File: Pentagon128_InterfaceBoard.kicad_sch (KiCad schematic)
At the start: 35 parts, among them J1 DIN41612_02x32_AB, J10 Tape Out, J11 Tape In, J12 Mini-DIN-6, J13 Conn_02x05_Odd_Even ATmega Pr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, J14 Barrel_Jack_Switch, J2 Conn_02x03_Odd_Even ATmega Pr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, J3 Conn_02x08_Odd_Even Ext Keyb, J4 Conn_02x05_Odd_Even Kempston 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, J5 DE9_Plug Kempston Out SMD, J6 DE15_Plug_HighDensity VGA CRT, J7 Conn_01x04 FDD Power, J8 Conn_01x04 Audio In, J9 AudioJack3, Q1 Q_NPN_BCE, Q2 Q_NPN_BCE, Q3 Q_NPN_BCE, Q4 Q_NPN_BCE, U1 MT8816 PLCC44, U2 ATmega168PA-A

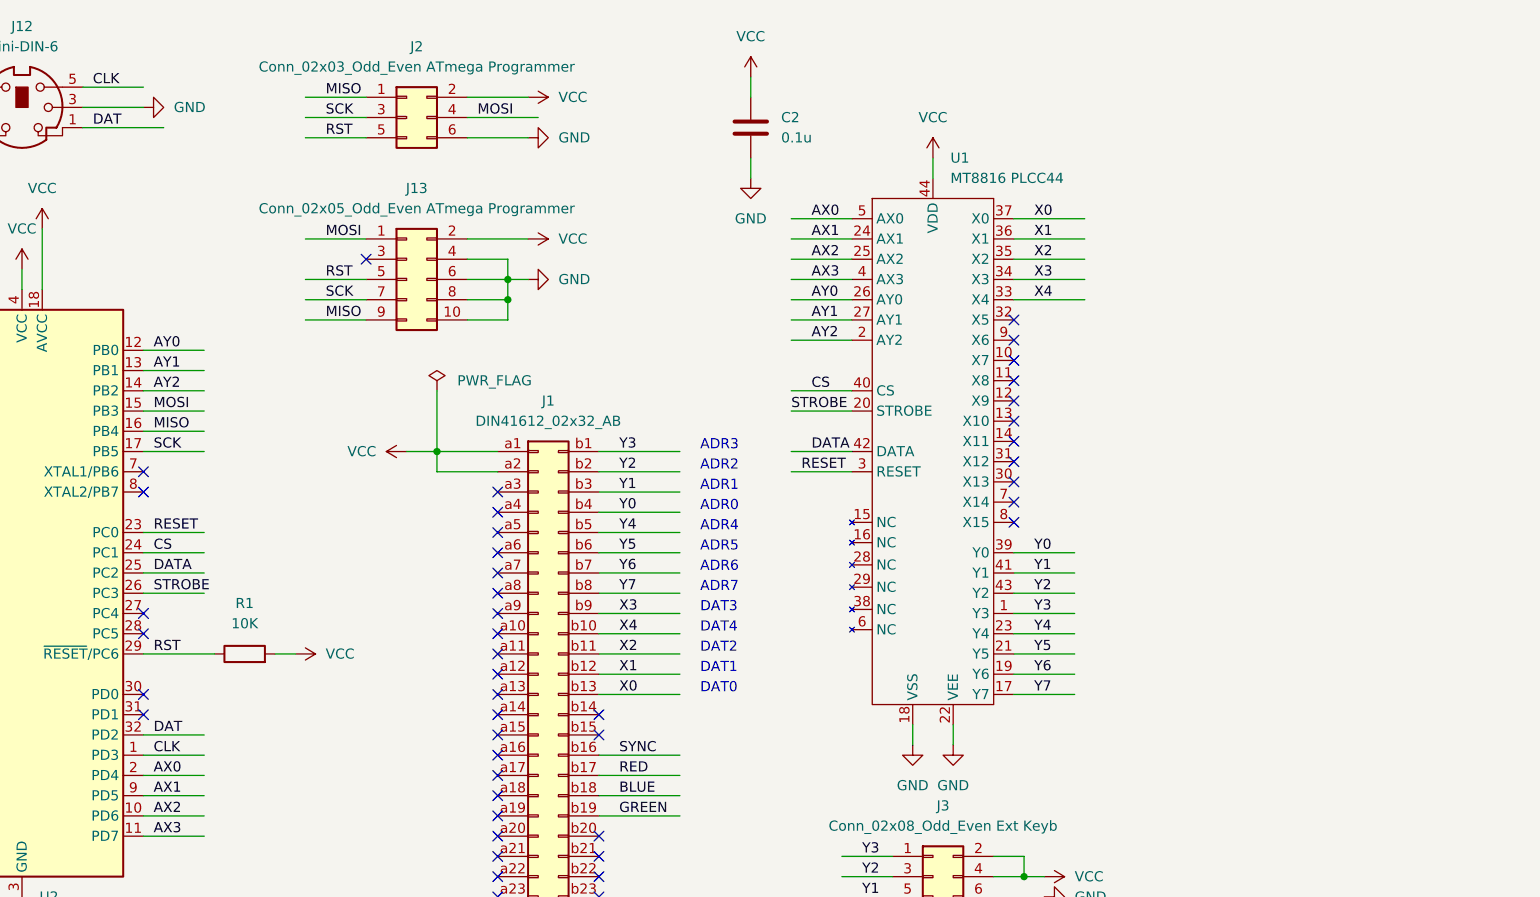
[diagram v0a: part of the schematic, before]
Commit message: Intermediate variant based on review feedback. Added SN74LS07 oped drain buffers for switch matrix data lines output (questionable). Changes based on "AVR Microcontroller Hardware Design Considerations": - Blocking capacitor for ATmega moved close to power input pins, removed side VCC / GND connections. Not implemented: separate blocking caps for AVCC and all power pins pairs. - Added optional capacitor on ATmega RESET line connected to GND. Removed useless blocking capacitor for MT8816. Removed (possibly) useless electrolytic capacitors from PCB near ATmega and FDC Power connector.
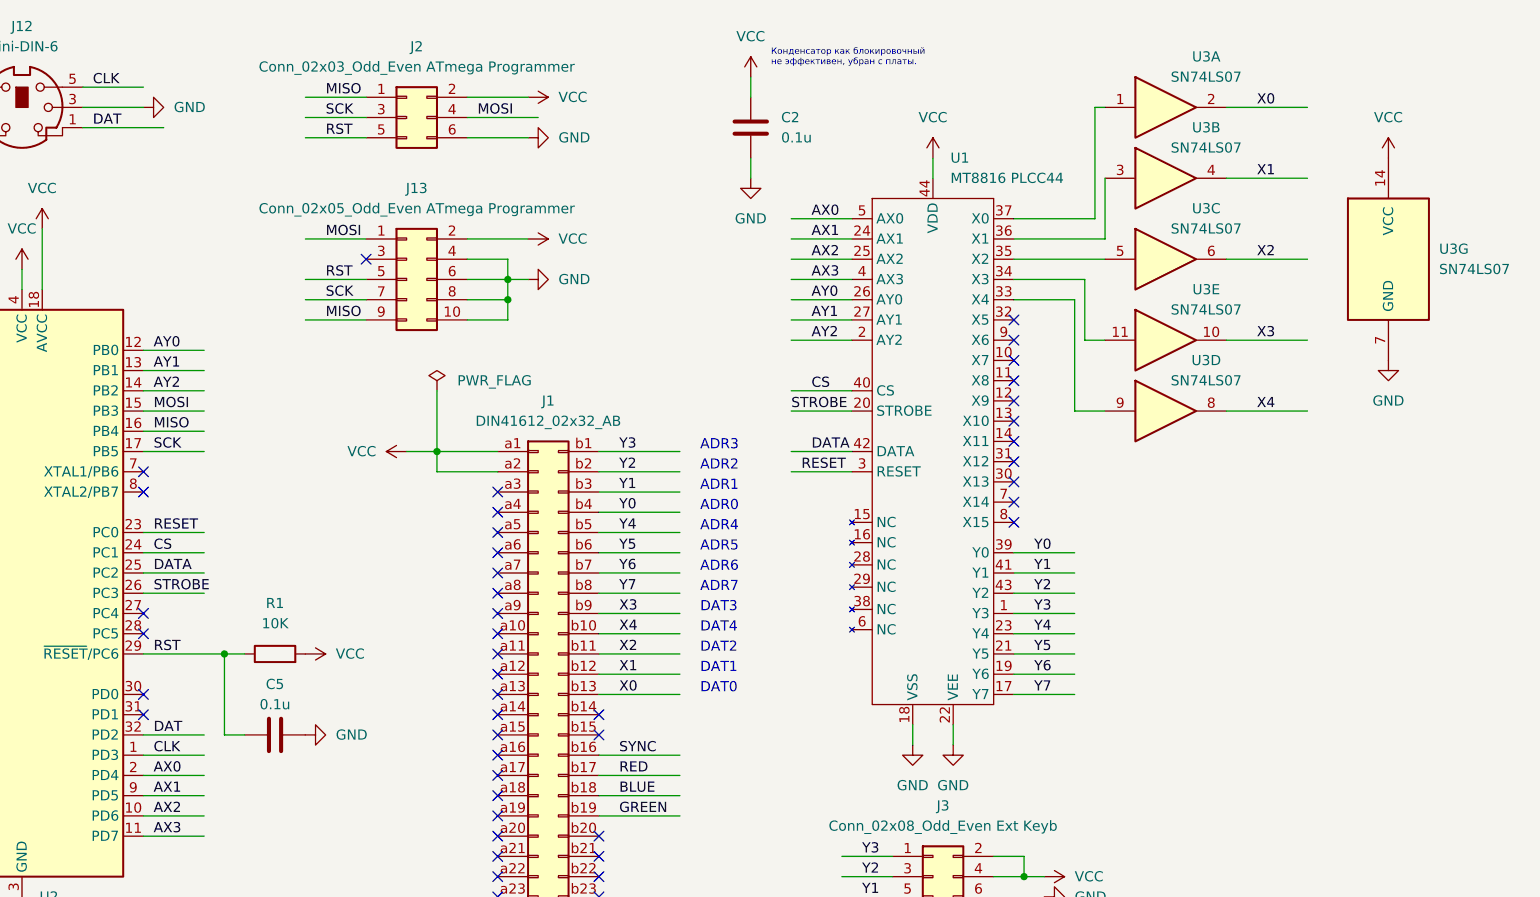
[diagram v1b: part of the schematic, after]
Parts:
- added C5: 0.1u, Capacitor_SMD:C_1206_3216Metric_Pad1.33x1.80mm_HandSolder, symbol Device:C
- added U3: SN74LS07, Package_SO:SOIC-14_3.9x8.7mm_P1.27mm, symbol 74xx:SN74LS07
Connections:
- net GND: now also C5.2, U3.7 (GND)
- net RST: now also C5.1
- net VCC: now also U3.14 (VCC)
- net X0: now also U3.2; no longer U1.37 (X0)
- net X1: now also U3.4; no longer U1.36 (X1)
- net X2: now also U3.6; no longer U1.35 (X2)
- net X3: now also U3.10; no longer U1.34 (X3)
- net X4: now also U3.8; no longer U1.33 (X4)
- new net: U1.37 (X0), U3.1
- new net: U1.35 (X2), U3.5
- new net: U1.33 (X4), U3.9
- new net: U1.34 (X3), U3.11
- new net: U1.36 (X1), U3.3
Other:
- note added: "Конденсатор как блокировочный не эффективен, убран с платы."
- moved on the sheet: R1

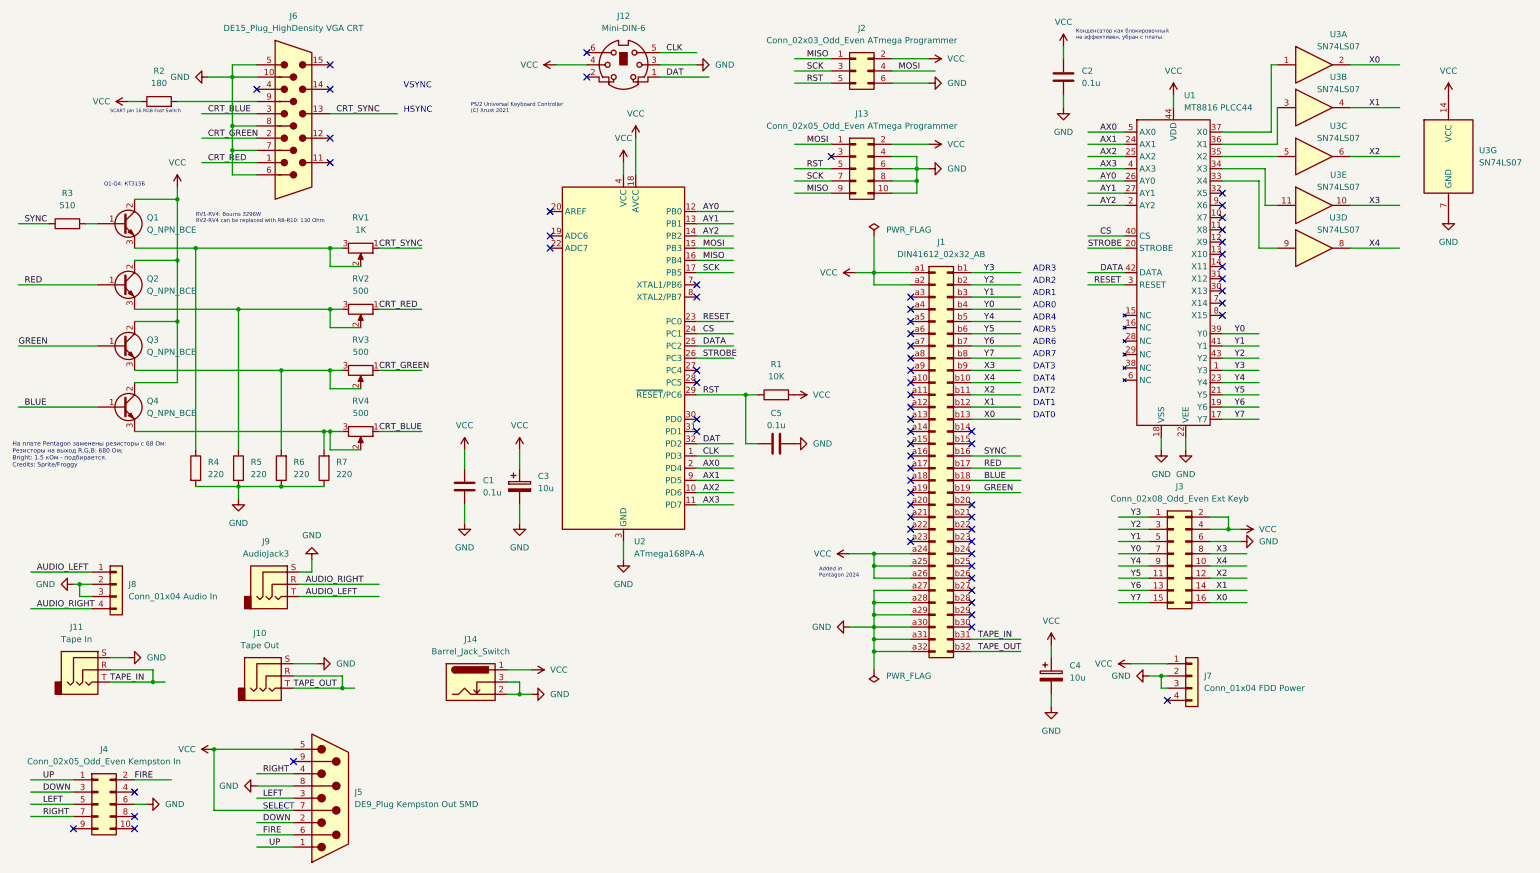
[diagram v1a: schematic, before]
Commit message: Remove SN74LS07 data bus buffer from schematic and PCB, considering MT8816 switches as switches connecting logical "0" from address bus line to keyboard data bus pulled to "1" (VCC) via pull-up resistors. There is no direct connections of address bus lines to VCC ("1") because of diodes.
Re-enumerate capacitors.
Remove electrolytic capacitors from board.
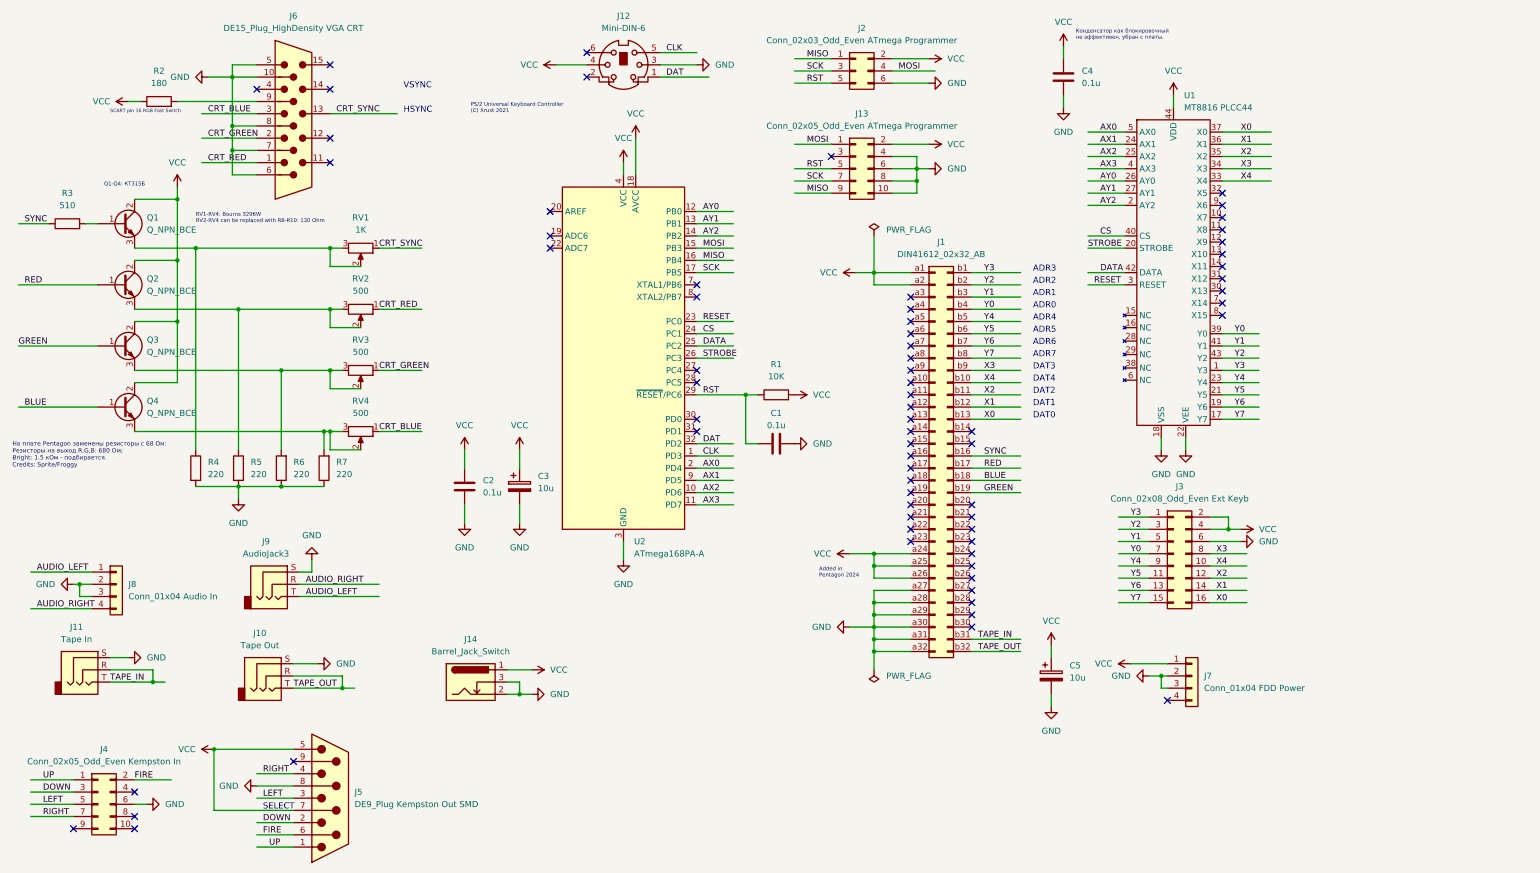
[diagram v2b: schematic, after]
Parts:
- removed U3: SN74LS07, Package_SO:SOIC-14_3.9x8.7mm_P1.27mm, symbol 74xx:SN74LS07
- renumbered C5 to C1, C1 to C2, C2 to C4, C4 to C5
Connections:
- net X0: now also U1.37 (X0)
- net X1: now also U1.36 (X1)
- net X2: now also U1.35 (X2)
- net X3: now also U1.34 (X3)
- net X4: now also U1.33 (X4)

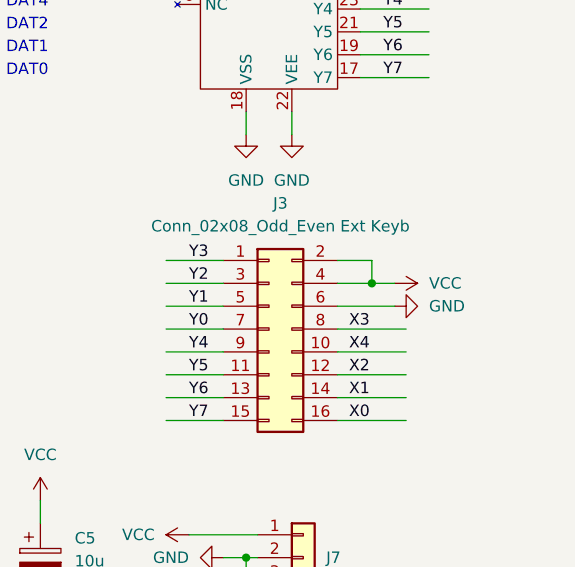
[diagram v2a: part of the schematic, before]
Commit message: Replace MT8816 pin solder footprint with PLCC-44_THT-Socket.
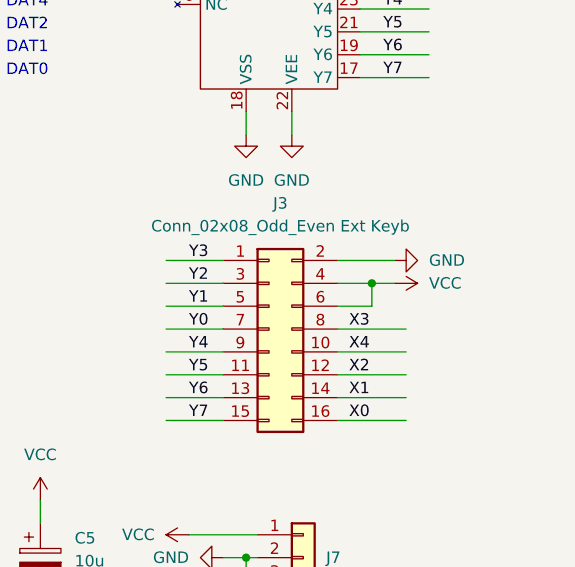
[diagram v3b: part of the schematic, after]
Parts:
- U1: footprint Package_LCC:PLCC-44 -> Package_LCC:PLCC-44_THT-Socket
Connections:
- net GND: now also J3.2 (Pin_2); no longer J3.6 (Pin_6)
- net VCC: now also J3.6 (Pin_6); no longer J3.2 (Pin_2)

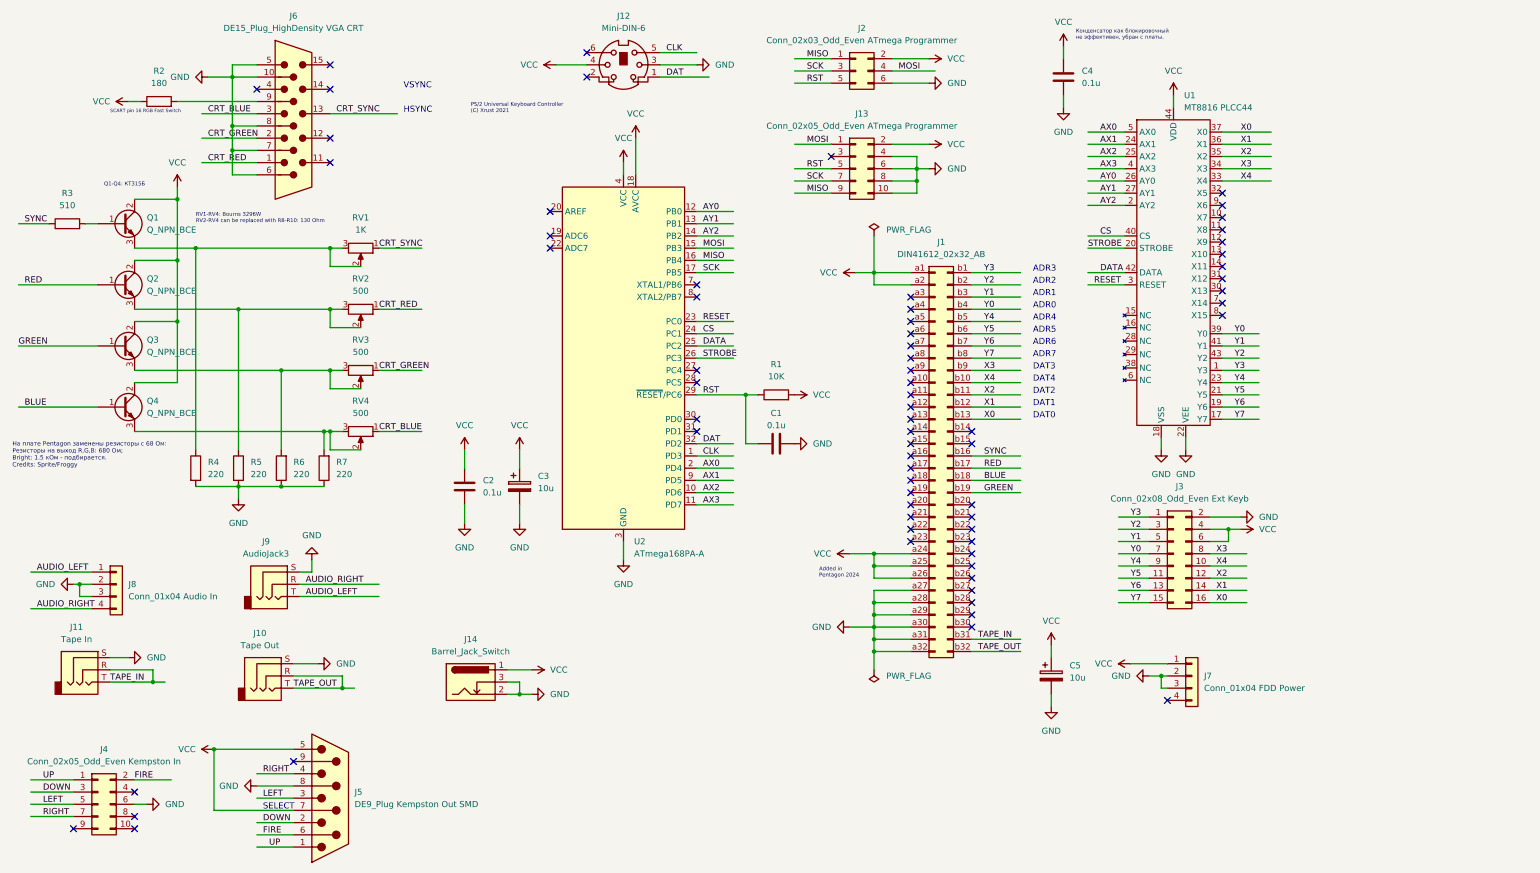
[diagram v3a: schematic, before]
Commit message: Add VGA output based on @Alex_Eburg's https://github.com/AlexEkb4ever/ZX_RGBI2VGA-HDMI Repace Raspberry Pi Pico with RP2040-Zero. Add 9 pin RGBI header for Pentagon 2023. Add RP2040-Zero symbol and footprint.
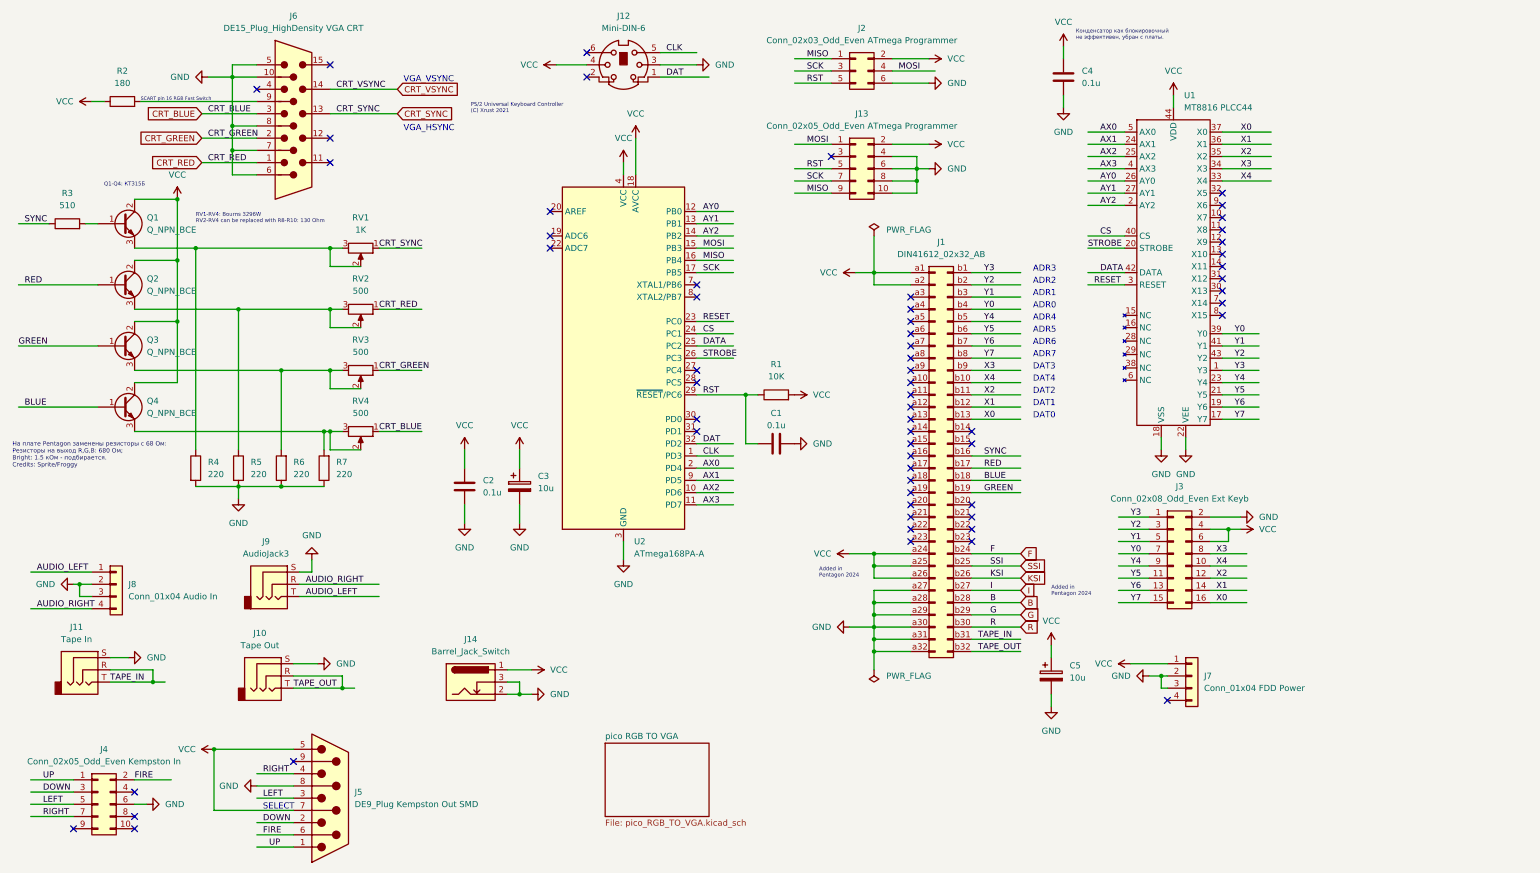
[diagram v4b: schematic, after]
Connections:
- net F: now reaches J1.b24 (Pin_b24)
- net SSI: now reaches J1.b25 (Pin_b25)
- net KSI: now reaches J1.b26 (Pin_b26)
- net I: now reaches J1.b27 (Pin_b27)
- net B: now reaches J1.b28 (Pin_b28)
- net G: now reaches J1.b29 (Pin_b29)
- net R: now reaches J1.b30 (Pin_b30)
- net CRT_VSYNC: now reaches J6.14
- no-connect marks 68 -> 60
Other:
- added sheet pico RGB TO VGA (pico_RGB_TO_VGA.kicad_sch)
- note added: "VGA_HSYNC"
- note added: "VGA_VSYNC"
- note removed: "HSYNC"
- note removed: "VSYNC"
- moved on the sheet: R2
